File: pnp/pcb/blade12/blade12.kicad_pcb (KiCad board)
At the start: 2 copper layers, 185 x 26.6 mm, 50 parts, among them J10 SPRING_PINS, J11 SPRING_PINS, J12 SPRING_PINS, J13 SPRING_PINS, J14 SPRING_PINS, J15 SPRING_PINS, J2 SPRING_PINS, J3 IN, J4 OUT, J5 SPRING_PINS, J6 SPRING_PINS, J7 SPRING_PINS, J8 SPRING_PINS, J9 SPRING_PINS, U1 DS28E07, U10 DS28E07, U11 DS28E07, U12 DS28E07, U2 DS28E07, U3 DS28E07, U4 DS28E07, U5 DS28E07, U6 DS28E07, U7 DS28E07, U8 DS28E07, U9 DS28E07

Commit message: updates blades
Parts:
- moved kibuzzard-65FDD87B 4.97 mm to (119.5, 55.0)
- moved kibuzzard-65FDD8A5 2.29 mm to (120.2, 60.2)
- moved kibuzzard-65FDD860 0.85 mm to (109.5, 50.0)

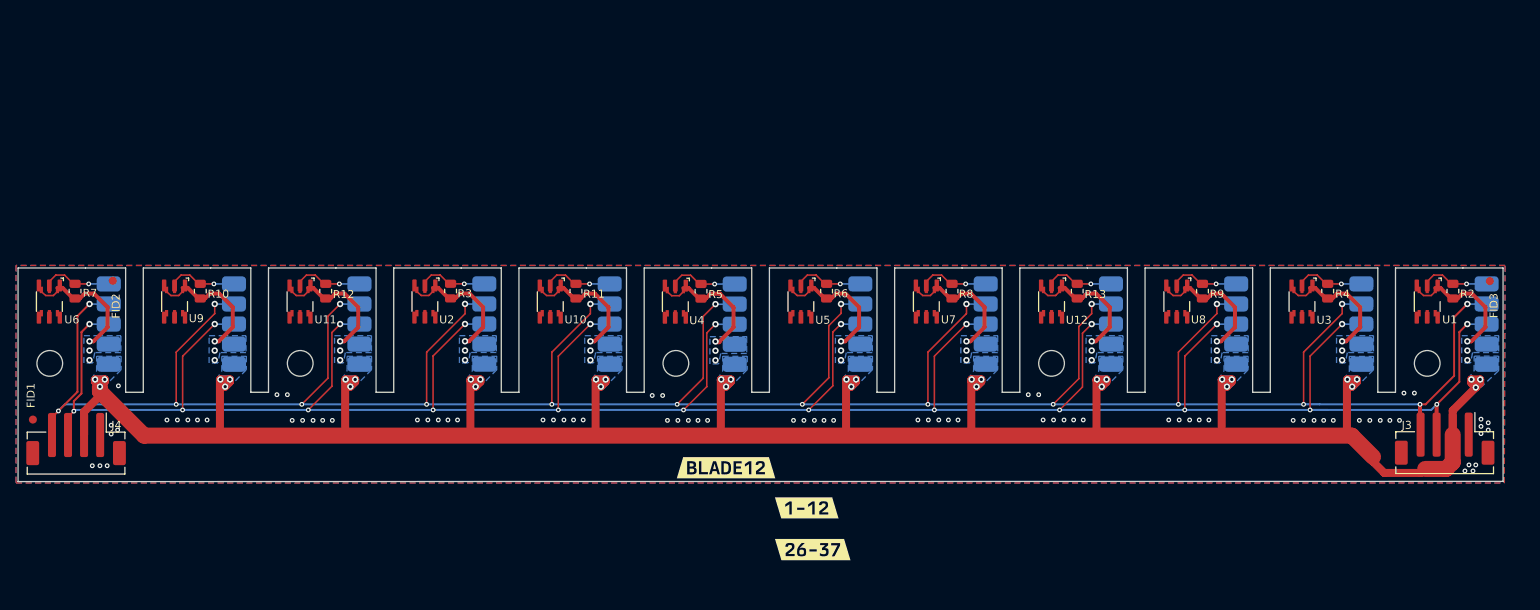
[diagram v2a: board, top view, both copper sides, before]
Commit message: adds slightly larger spaced blade pcb, plus a slightly increased 13 blade print. still needs 12
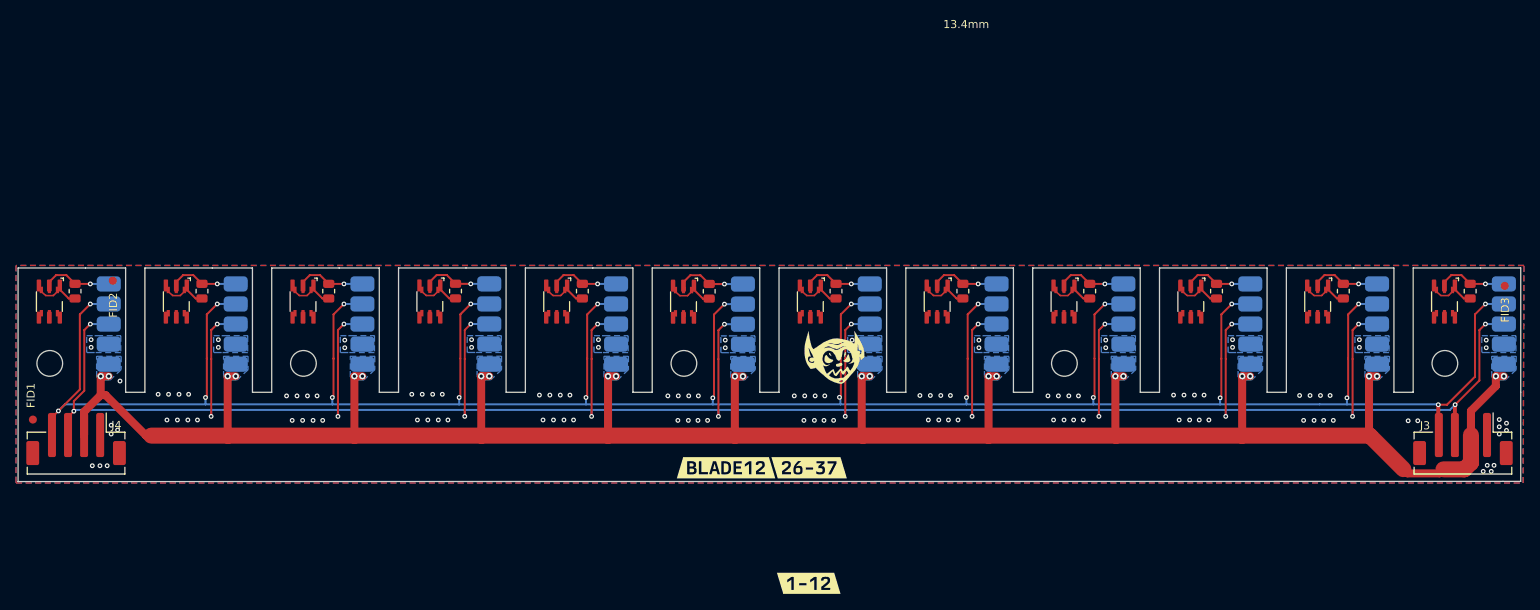
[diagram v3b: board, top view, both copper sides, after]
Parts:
- moved kibuzzard-65FDD8A5 10.2 mm to (119.8, 50.0)
- moved kibuzzard-65FDD87B 9.40 mm to (119.8, 64.4)
- moved G*** 4.10 mm to (123.0, 36.7), turned to 5 degrees
- moved J3 2.28 mm to (201.2, 46.4)
- moved H5 2.20 mm to (199.0, 37.0)
- moved U1 2.15 mm to (199.0, 29.3)
- moved J2 2.15 mm to (206.3, 27.1)
- moved R2 2.15 mm to (202.2, 28.0)
- moved U3 1.95 mm to (183.2, 29.3)
- moved J6 1.95 mm to (190.6, 27.1)
- moved R4 1.95 mm to (186.3, 28.0)
- moved FID3 1.94 mm to (206.4, 27.4)
- moved U8 1.75 mm to (167.4, 29.3)
- moved J11 1.75 mm to (174.8, 27.1)
- moved R9 1.75 mm to (170.6, 28.0)
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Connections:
- J3 pad MP: (no net) -> GND
- J4 pad MP: (no net) -> GND
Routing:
- net GND: track 158.7 -> 32.3 mm, vias 115 -> 122
- net VIN: track 311.3 -> 281.7 mm, vias 36 -> 24
- net RS-485+: track 382.5 -> 368.7 mm
- net RS-485-: track 354.5 -> 356.5 mm
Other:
- board size 185 x 26.6 mm -> 187.2 x 26.6 mm
- board text added: "13.4mm"
